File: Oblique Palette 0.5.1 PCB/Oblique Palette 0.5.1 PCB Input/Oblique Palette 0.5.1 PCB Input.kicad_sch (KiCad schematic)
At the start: 19 parts, among them J15 Conn_01x03_Male_Pin, J16 Conn_01x03_Female_Pin, J17 AudioJack2_SwitchT, U3 MCP6004

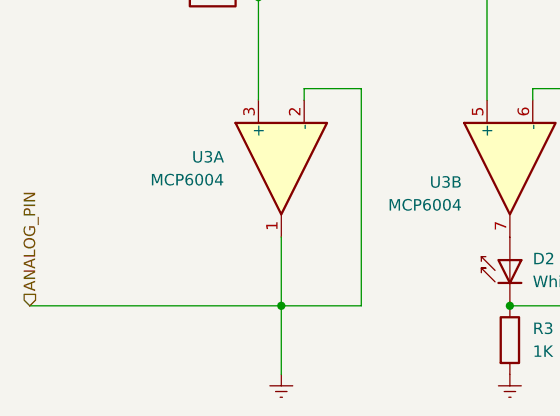
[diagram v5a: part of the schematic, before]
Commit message: Re-routed with many errors fixed
Found some unplaced resistors necessary for bringing output control voltages down to LED levels.
Eliminated artifacts of previous drafts.
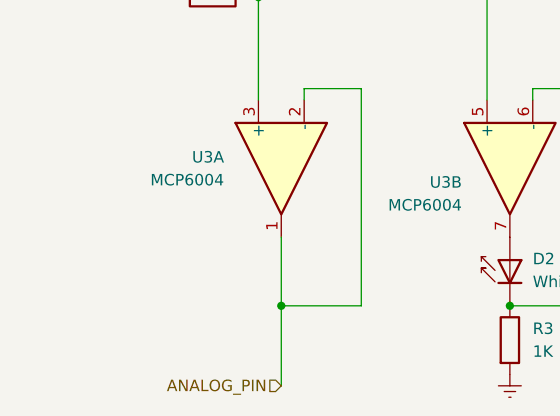
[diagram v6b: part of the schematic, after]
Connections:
- net GNDREF: no longer U3.1, U3.2 (-)
- new net ANALOG_PIN: U3.1, U3.2 (-)
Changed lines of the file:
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@@
 	(wire
 		(pts
-			(xy 77.47 120.65) (xy 105.41 120.65)
+			(xy 97.79 63.5) (xy 99.06 63.5)
 		)
 		(stroke
@@
 	(wire
 		(pts
-			(xy 97.79 63.5) (xy 99.06 63.5)
+			(xy 105.41 129.54) (xy 105.41 120.65)
 		)
 		(stroke
@@
 	(wire
 		(pts
-			(xy 105.41 120.65) (xy 105.41 128.27)
-		)
-		(stroke
-			(width 0)
-			(type default)
-		)
-	)
-	(wire
-		(pts
 			(xy 176.53 87.63) (xy 176.53 97.79)
 		)
@@
 	(hierarchical_label "ANALOG_PIN"
 		(shape input)
-		(at 77.47 120.65 90)
+		(at 105.41 129.54 180)
 		(effects
 			(font
 				(size 1.27 1.27)
 			)
-			(justify left)
+			(justify right)
 		)
 	)
@@
 					(unit 1)
 				)
-			)
-		)
-	)
-	(symbol
-		(lib_id "power:GNDREF")
-		(at 105.41 128.27 0)
-		(unit 1)
-		(exclude_from_sim no)
-		(in_bom yes)
-		(on_board yes)
-		(dnp no)
-		(fields_autoplaced yes)
-		(property "Reference" "#PWR068"
-			(at 105.41 134.62 0)
-			(effects
-				(font
-					(size 1.27 1.27)
-				)
-				(hide yes)
-			)
-		)
-		(property "Value" "GNDREF"
-			(at 105.41 133.35 0)
-			(effects
-				(font
-					(size 1.27 1.27)
-				)
-				(hide yes)
-			)
-		)
-		(property "Footprint" ""
-			(at 105.41 128.27 0)
-			(effects
-				(font
-					(size 1.27 1.27)
-				)
-				(hide yes)
-			)
-		)
-		(property "Datasheet" ""
-			(at 105.41 128.27 0)
-			(effects
-				(font
-					(size 1.27 1.27)
-				)
-				(hide yes)
-			)
-		)
-		(property "Description" "Power symbol creates a global label with name \"GNDREF\" , reference supply ground"
-			(at 105.41 128.27 0)
-			(effects
-				(font
-					(size 1.27 1.27)
-				)
-				(hide yes)
-			)
-		)
-		(pin "1"
-		)
-		(instances
-			(project "Oblique Palette 0.4 Input Stage"
-				(path "/150b6f87-53bb-44d6-889a-48fbcb7c0f5a"
-					(reference "#PWR?")
-					(unit 1)
-				)
-			)
-			(project "Oblique Palette 0.5.1 PCB Main"
-				(path "/28718c51-05fa-44bf-9e59-30883fb9ecef/10bc258e-81e1-44f3-990d-192650ef1d17"
-					(reference "#PWR0119")
-					(unit 1)
-				)
-				(path "/28718c51-05fa-44bf-9e59-30883fb9ecef/57e02da9-4257-4ca7-873b-16131b7a2160"
-					(reference "#PWR085")
-					(unit 1)
-				)
-				(path "/28718c51-05fa-44bf-9e59-30883fb9ecef/7745d2af-7356-4abb-bb12-892bad795ddc"
-					(reference "#PWR0187")
-					(unit 1)
-				)
-				(path "/28718c51-05fa-44bf-9e59-30883fb9ecef/987e670c-6148-4b51-9cfd-5f14311b6128"
-					(reference "#PWR0170")
-					(unit 1)
-				)
-				(path "/28718c51-05fa-44bf-9e59-30883fb9ecef/b5a2c36a-8809-438c-979e-3df70d5c3577"
-					(reference "#PWR0153")
-					(unit 1)
-				)
-				(path "/28718c51-05fa-44bf-9e59-30883fb9ecef/b606fcb4-531c-4aac-8b9c-456946edc41a"
-					(reference "#PWR0102")
-					(unit 1)
-				)
-				(path "/28718c51-05fa-44bf-9e59-30883fb9ecef/f139377a-d7a4-4f83-81e4-8f98ca8ad38f"
-					(reference "#PWR068")
-					(unit 1)
-				)
-				(path "/28718c51-05fa-44bf-9e59-30883fb9ecef/f541c48a-fb18-4fa4-aa45-9d69b2f53442"
-					(reference "#PWR0136")
-					(unit 1)
-				)

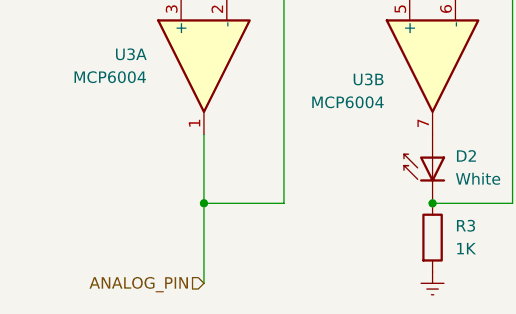
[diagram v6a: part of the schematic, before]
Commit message: Fixing input channels
Issues:
1. Some (all?) input channels are not connected to the multiplexer. This seems to be an issue with my hierarchical labels?
2. Input op amps do not seem to have inputs for the yellow and red LEDs. Again, they seem to be disconnected.

Checked: levels coming out of the potentiometers are correct.
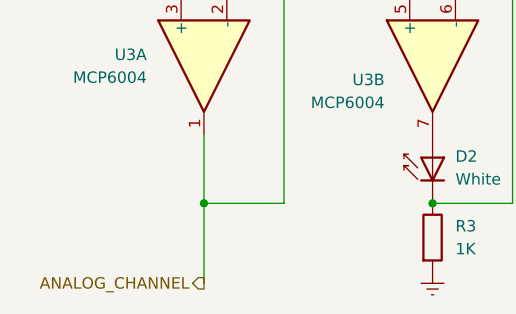
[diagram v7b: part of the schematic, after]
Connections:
- net ANALOG_PIN renamed ANALOG_CHANNEL
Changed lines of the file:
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@@
 		)
 	)
-	(hierarchical_label "ANALOG_PIN"
-		(shape input)
+	(hierarchical_label "ANALOG_CHANNEL"
+		(shape output)
 		(at 105.41 129.54 180)
 		(effects

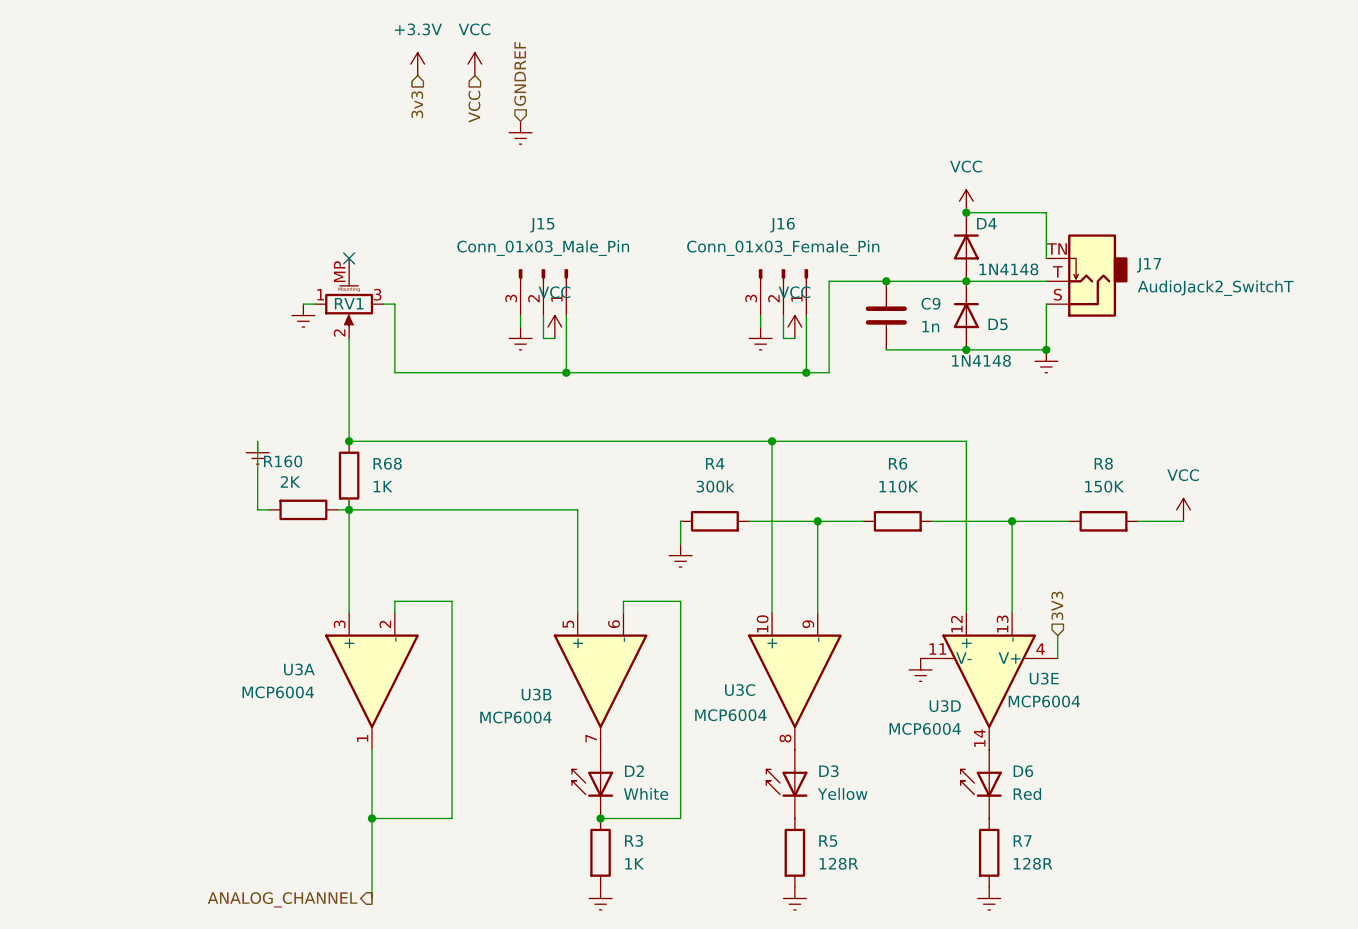
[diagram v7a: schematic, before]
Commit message: All traces(?) now connected on PCB.
This is looking good to me. Vcc and VServo are merged for simplicity. Not the best solution. I think maybe a breakable trace or a single jumper might be the way to do this.
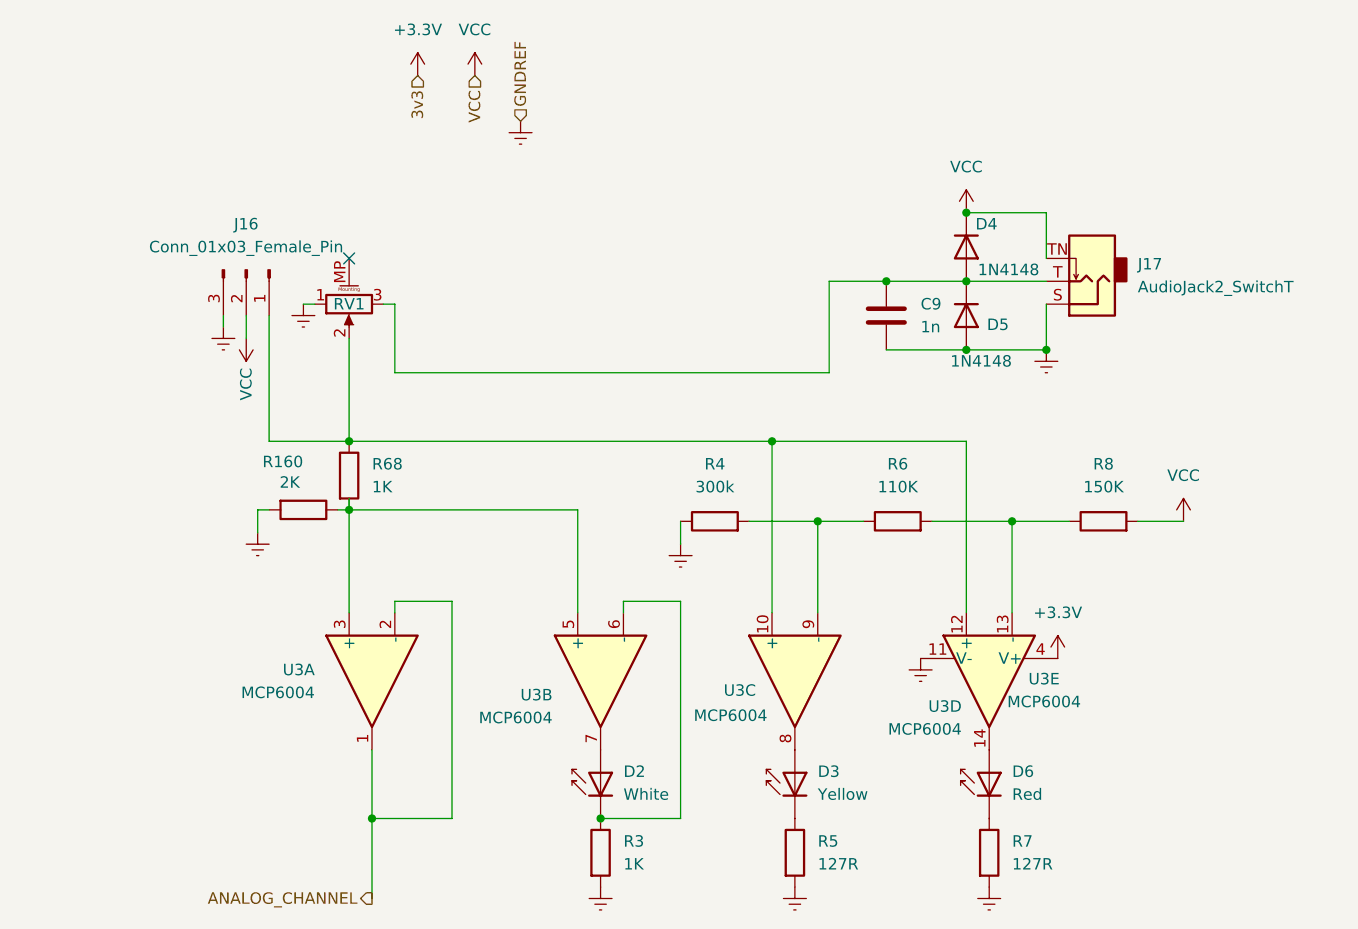
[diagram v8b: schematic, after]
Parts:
- removed J15: Conn_01x03_Male_Pin, Connector_PinHeader_2.54mm:PinHeader_1x03_P2.54mm_Vertical, symbol Connector:Conn_01x03_Pin
- R5, R7: value 128R -> 127R
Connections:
- net 3V3 is gone; now on net +3.3V: U3.4 (V+)
- net at C9.1, D4.2 (A), D5.1 (K)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: no longer J16.1 (Pin_1)
- net at R68.1, RV1.2, U3.10 (+)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: now also J16.1 (Pin_1)
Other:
- moved on the sheet: J16
